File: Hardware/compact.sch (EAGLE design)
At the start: 22 parts, among them SW1 SWITCH_SPDT, U1 MCP73831, U2 EDISON_CONNECTOR_FULLMOUNTING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, U3 EDISON_CONNECTOR_FULLHEADER

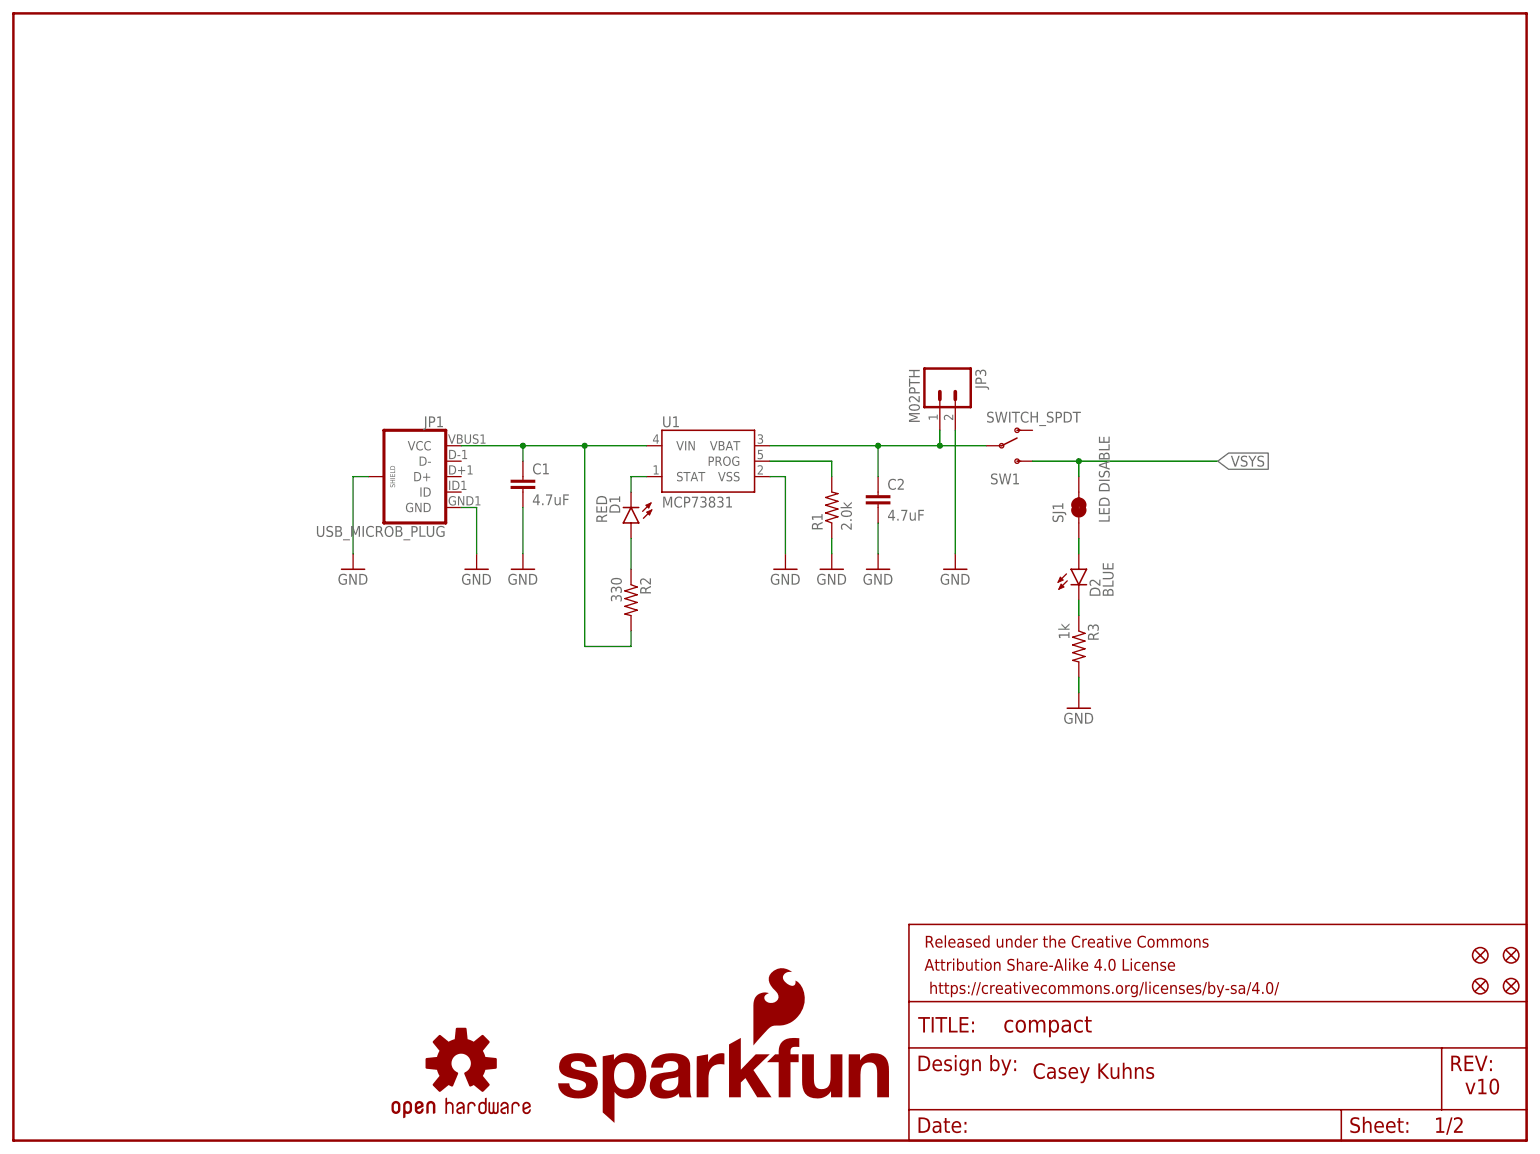
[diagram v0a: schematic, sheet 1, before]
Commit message: Initial HP95LX daughterboard layouts
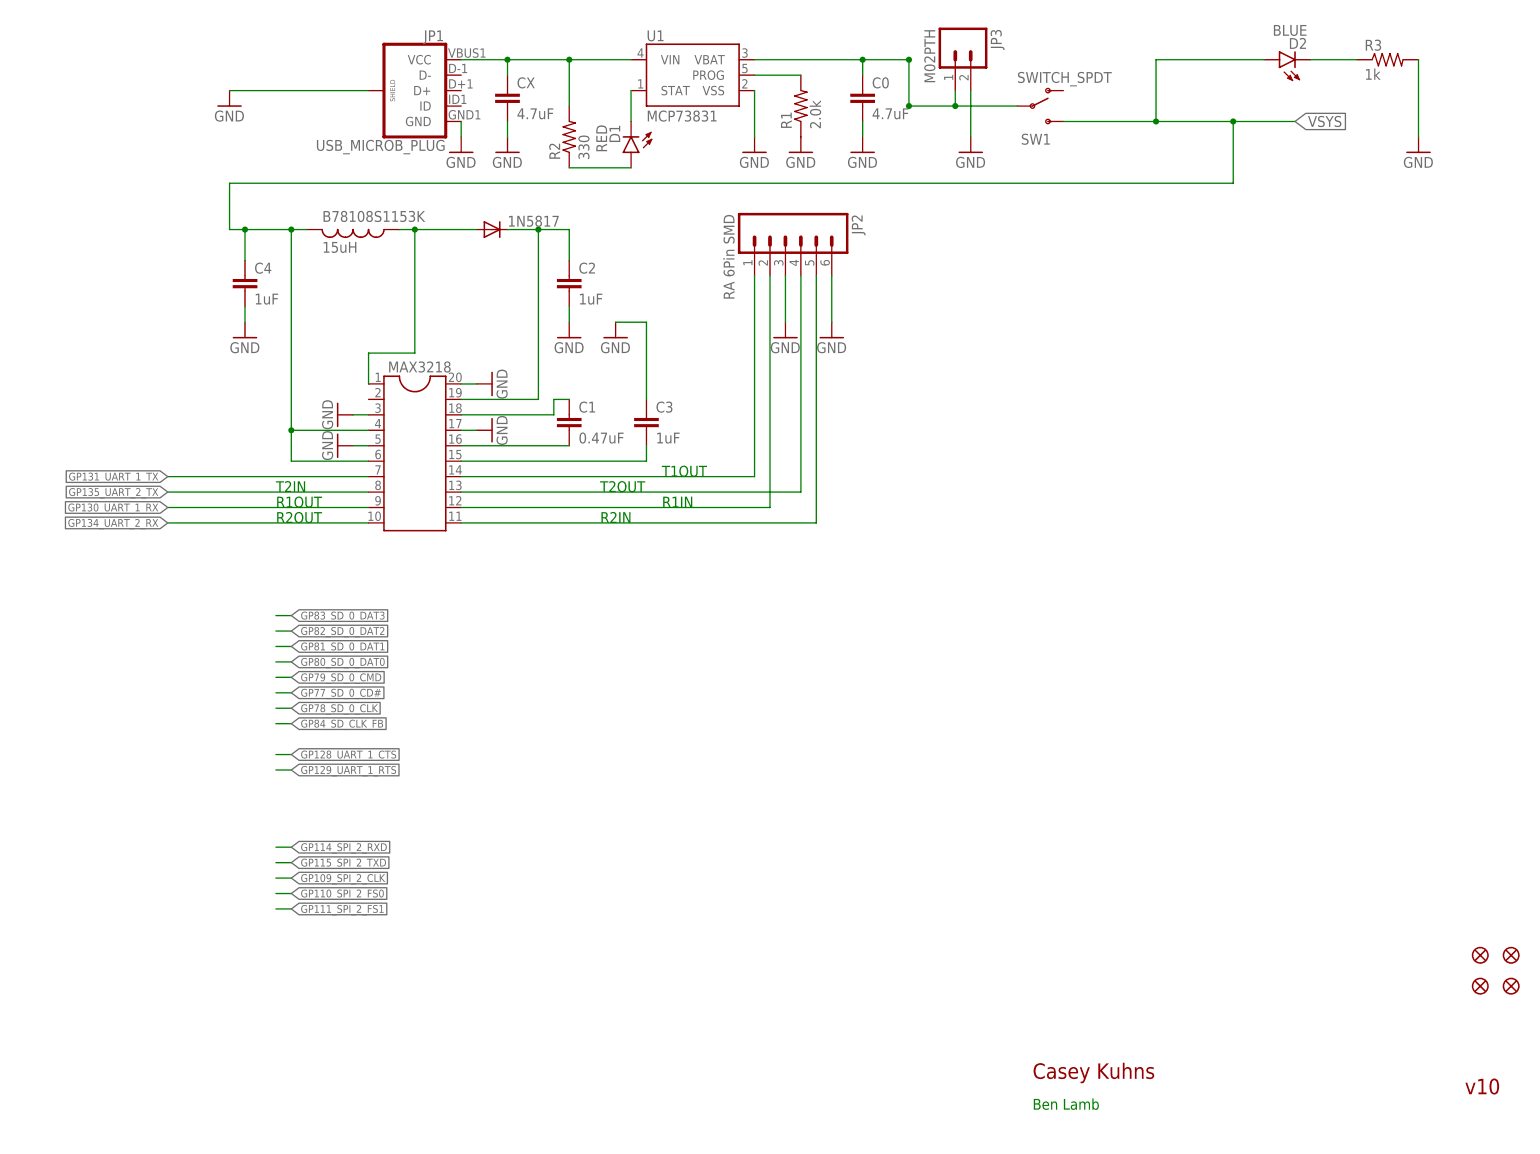
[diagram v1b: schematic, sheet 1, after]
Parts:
- removed FRAME1: FRAME-LETTER, SparkFun-Aesthetics:FRAME-LETTER
- removed LOGO1: OSHW-LOGOS, SparkFun-Aesthetics:OSHW-LOGOS
- removed LOGO4: SFE_LOGO_NAME_FLAME.1_INCH, SparkFun-Aesthetics:SFE_LOGO_NAME_FLAME.1_INCH
- removed SJ1: LED DISABLE, SparkFun-Passives:JUMPER-PAD-2-NC_BY_TRACE
- added 1N5817: (no value), diode:DIODE-DO41-10
- added B78108S1153K: 15uH, resistor:L-US0207/15
- added C0, CX: 4.7uF, SparkFun-Capacitors:4.7UF-6.3V-10%(0603)0603
- added C3, C4: 1uF, SparkFun-Capacitors:CAPPTH1
- added JP2: RA 6Pin SMD, SparkFun-Connectors:M06SMD
- added MAX3218: (no value), ic-package:DIL20
- C1: value 4.7uF -> 0.47uF; device SparkFun-Capacitors:4.7UF-6.3V-10%(0603)0603 -> SparkFun-Capacitors:CAPPTH1
- C2: value 4.7uF -> 1uF; device SparkFun-Capacitors:4.7UF-6.3V-10%(0603)0603 -> SparkFun-Capacitors:CAPPTH1
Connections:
- removed net N$7: D2.A, SJ1.1
- removed net VIN: C1.1, JP1.VCC, R2.2, U1.VIN
- new net 1: 1N5817.A, B78108S1153K.1, MAX3218.1
- new net CX: CX.1, JP1.VCC, R2.2, U1.VIN
- new net N$10: JP2.4, MAX3218.13
- new net N$11: JP2.2, MAX3218.12
- new net N$13: JP2.5, MAX3218.11
- new net N$14: 1N5817.C, C2.1, MAX3218.19
- new net N$6: C3.2, MAX3218.15
- new net N$8: C1.1, MAX3218.18
- new net N$9: C1.2, MAX3218.16
- new net T1OUT: JP2.1, MAX3218.14
- net GND: now also C0.2, C3.1, C4.2, CX.2, JP2.3, JP2.6, MAX3218.17, MAX3218.20, MAX3218.3, MAX3218.5; no longer C1.2
- net GP130_UART_1_RX: now also MAX3218.9
- net GP131_UART_1_TX: now also MAX3218.7
- net GP134_UART_2_RX: now also MAX3218.10
- net GP135_UART_2_TX: now also MAX3218.8
- net VBAT: now also C0.1; no longer C2.1
- net VSYS: now also B78108S1153K.2, C4.1, D2.A, MAX3218.4, MAX3218.6; no longer SJ1.2
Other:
- note added: "Ben Lamb"
- note added: "R1IN"
- note added: "R1OUT"
- note added: "R2IN"
- note added: "R2OUT"
- note added: "T1OUT"
- note added: "T2IN"
- note added: "T2OUT"
- moved on the sheet: C1, C2, D1, D2, JP1, JP3, R1, R2, R3, SW1, U1
